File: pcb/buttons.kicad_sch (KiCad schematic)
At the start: 29 parts, among them SW1 SW_Push_SPDT, SW2 SW_Push_SPDT, SW3 SW_Push_SPDT, SW4 SW_Push_SPDT, SW5 RotaryEncoder

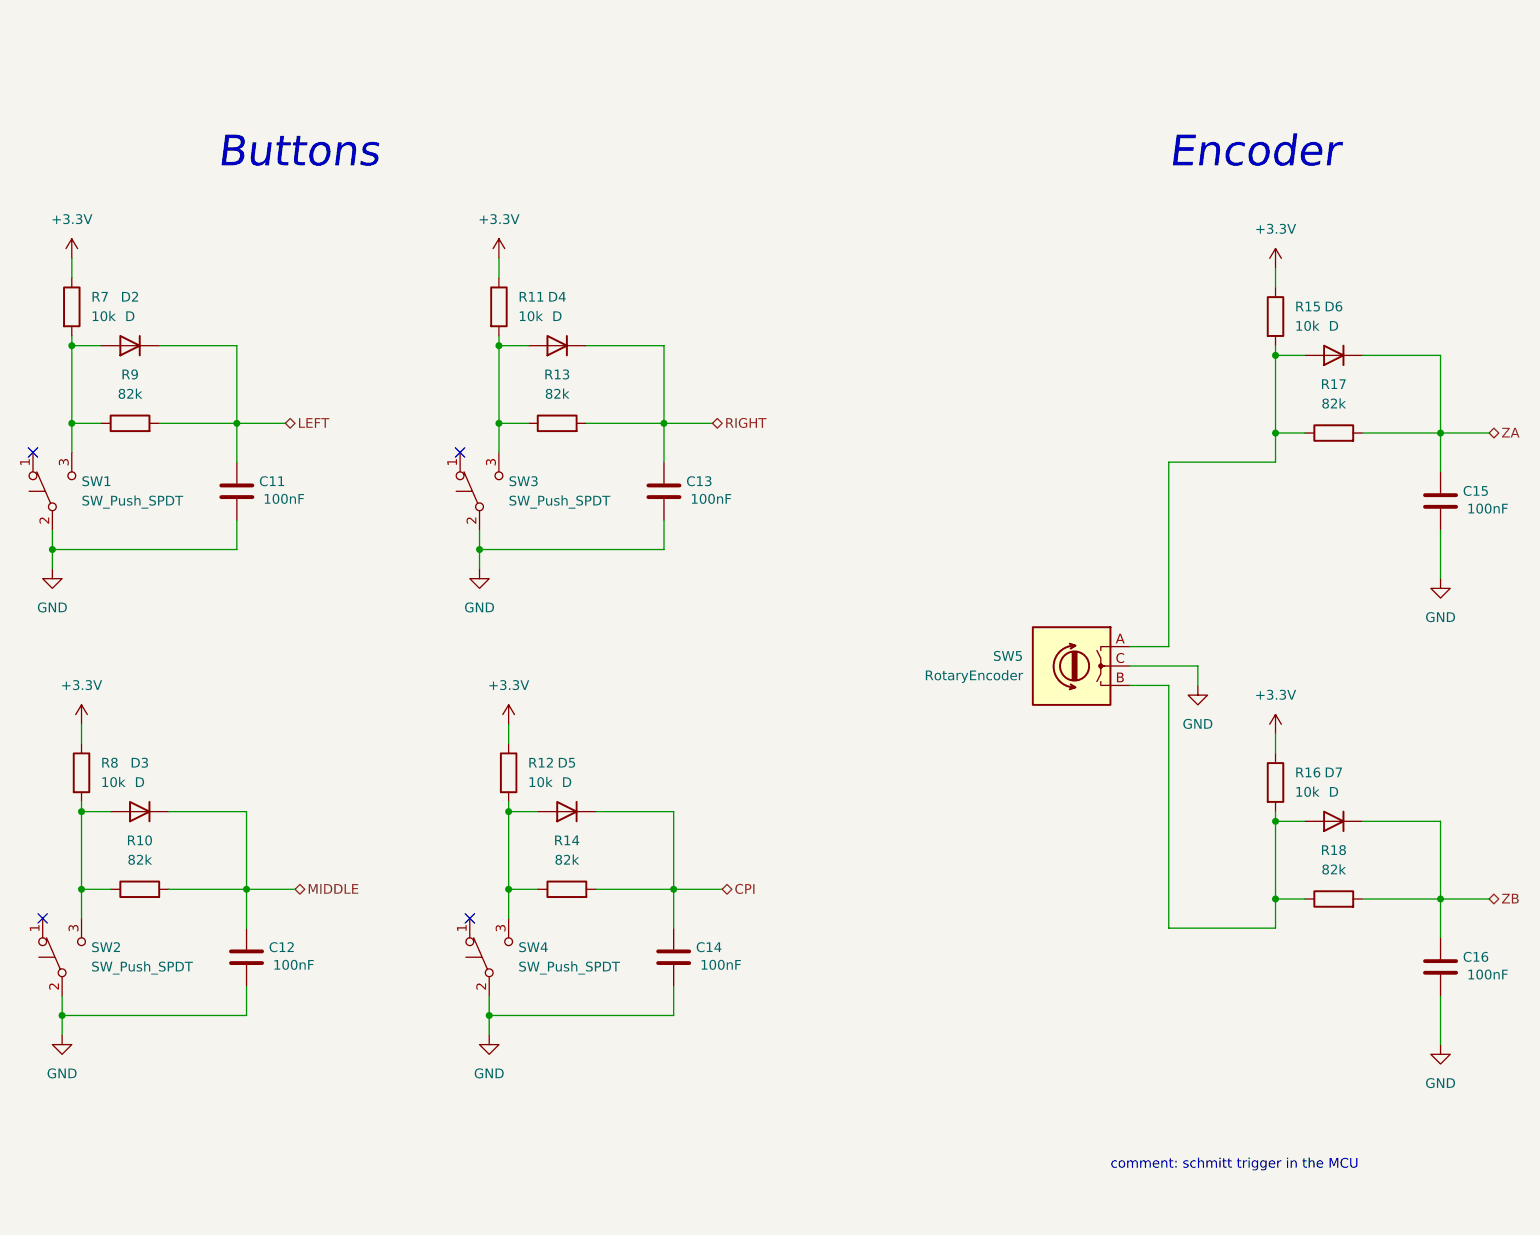
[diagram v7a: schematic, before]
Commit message: added PWR_FLAGs to pass ERC checks
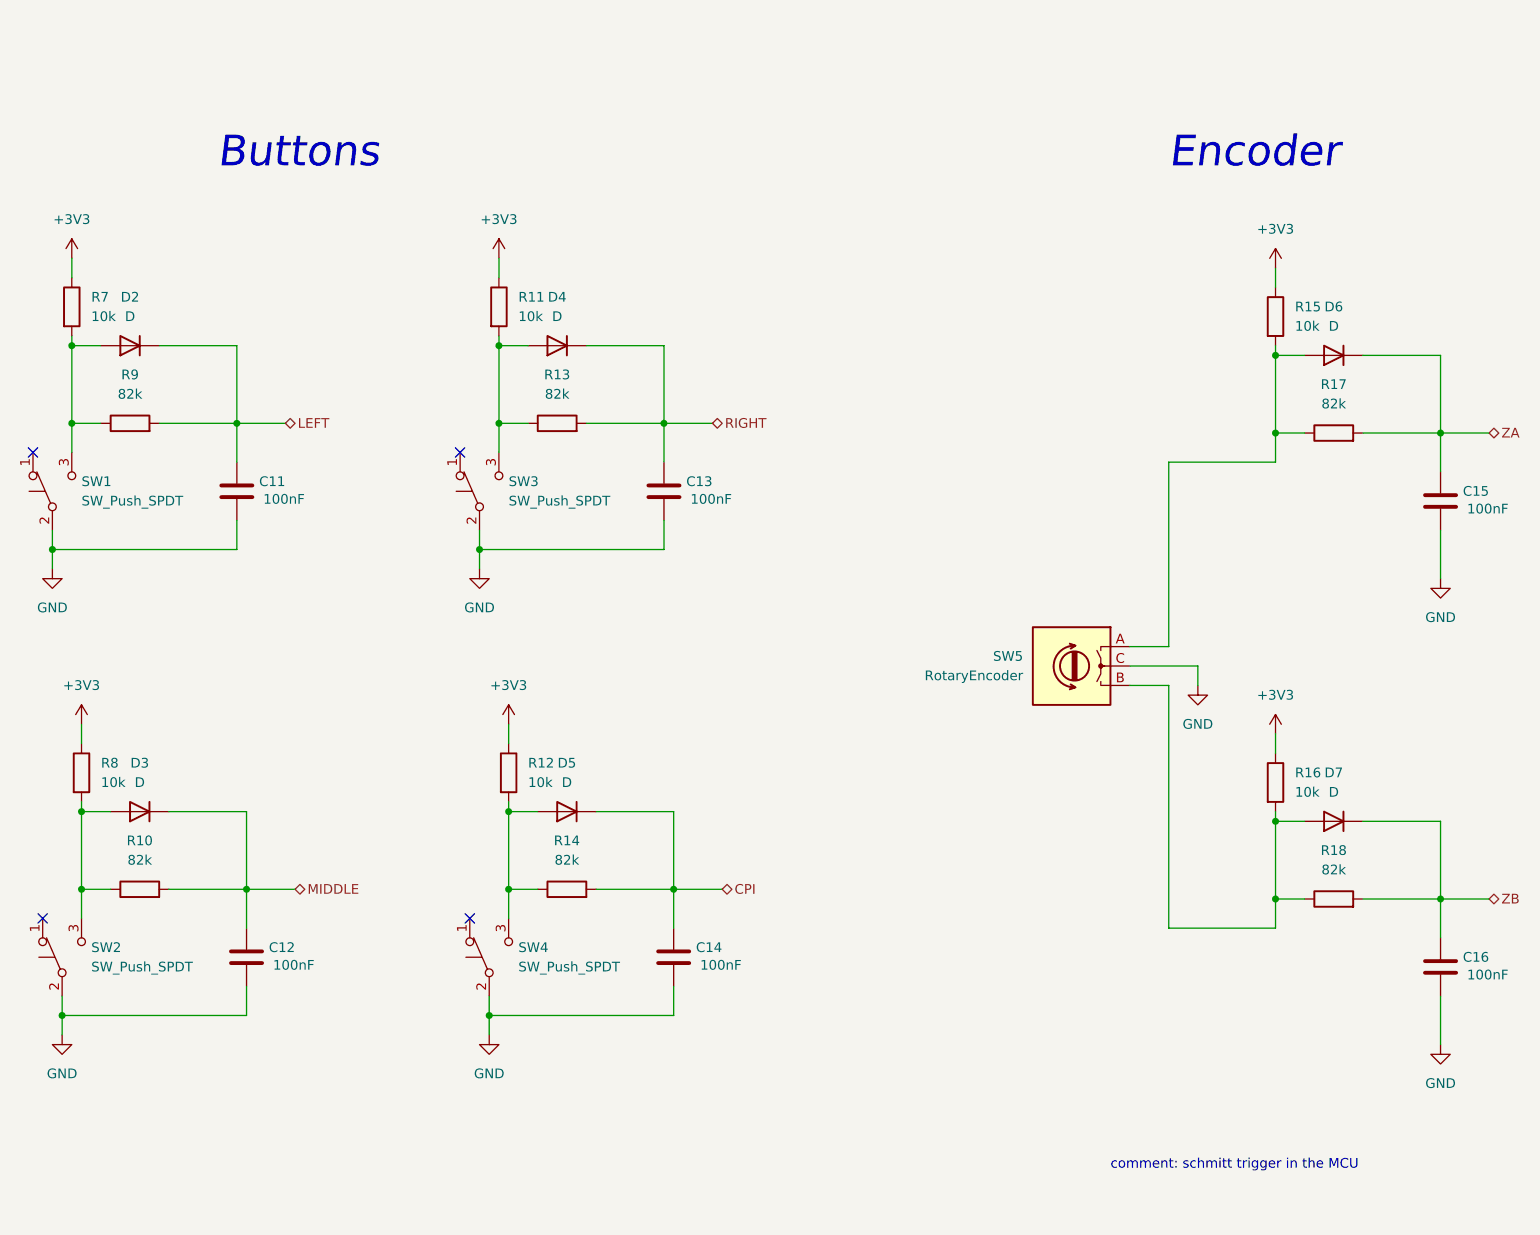
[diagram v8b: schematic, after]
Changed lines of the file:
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@@
     (stroke (width 0) (type default) (color 0 0 0 0))
   )
-  (wire (pts (xy 43.18 52.07) (xy 43.18 49.53))
+  (wire (pts (xy 43.18 49.53) (xy 43.18 52.07))
     (stroke (width 0) (type default) (color 0 0 0 0))
   )
@@
     (pin "1")
   )
+  (symbol (lib_id "power:+3V3") (at 200.66 50.8 0) (unit 1)
+    (in_bom yes) (on_board yes) (fields_autoplaced)
+    (property "Reference" "#PWR0105" (id 0) (at 200.66 54.61 0)
+      (effects (font (size 1.27 1.27)) hide)
+    )
+    (property "Value" "+3V3" (id 1) (at 200.66 45.72 0))
+    (property "Footprint" "" (id 2) (at 200.66 50.8 0)
+      (effects (font (size 1.27 1.27)) hide)
+    )
+    (property "Datasheet" "" (id 3) (at 200.66 50.8 0)
+      (effects (font (size 1.27 1.27)) hide)
+    )
+    (pin "1")
+  )
   (symbol (lib_id "power:GND") (at 222.25 152.4 0) (mirror y) (unit 1)
     (in_bom yes) (on_board yes)
@@
     (pin "2")
   )
-  (symbol (lib_id "power:+3.3V") (at 200.66 50.8 0) (unit 1)
-    (in_bom yes) (on_board yes) (fields_autoplaced)
-    (property "Reference" "#PWR032" (id 0) (at 200.66 54.61 0)
-      (effects (font (size 1.27 1.27)) hide)
-    )
-    (property "Value" "+3.3V" (id 1) (at 200.66 45.72 0))
-    (property "Footprint" "" (id 2) (at 200.66 50.8 0)
-      (effects (font (size 1.27 1.27)) hide)
-    )
-    (property "Datasheet" "" (id 3) (at 200.66 50.8 0)
-      (effects (font (size 1.27 1.27)) hide)
-    )
-    (pin "1")
-  )
   (symbol (lib_id "Device:C") (at 121.92 140.97 0) (mirror y) (unit 1)
     (in_bom yes) (on_board yes)
@@
     (pin "C")
   )
-  (symbol (lib_id "power:+3.3V") (at 99.06 49.53 0) (unit 1)
-    (in_bom yes) (on_board yes) (fields_autoplaced)
-    (property "Reference" "#PWR029" (id 0) (at 99.06 53.34 0)
-      (effects (font (size 1.27 1.27)) hide)
-    )
-    (property "Value" "+3.3V" (id 1) (at 99.06 44.45 0))
-    (property "Footprint" "" (id 2) (at 99.06 49.53 0)
-      (effects (font (size 1.27 1.27)) hide)
-    )
-    (property "Datasheet" "" (id 3) (at 99.06 49.53 0)
-      (effects (font (size 1.27 1.27)) hide)
-    )
-    (pin "1")
-  )
   (symbol (lib_id "Device:D") (at 52.07 121.92 180) (unit 1)
     (in_bom yes) (on_board yes) (fields_autoplaced)
@@
     (pin "2")
   )
+  (symbol (lib_id "power:+3V3") (at 100.33 110.49 0) (unit 1)
+    (in_bom yes) (on_board yes) (fields_autoplaced)
+    (property "Reference" "#PWR0101" (id 0) (at 100.33 114.3 0)
+      (effects (font (size 1.27 1.27)) hide)
+    )
+    (property "Value" "+3V3" (id 1) (at 100.33 105.41 0))
+    (property "Footprint" "" (id 2) (at 100.33 110.49 0)
+      (effects (font (size 1.27 1.27)) hide)
+    )
+    (property "Datasheet" "" (id 3) (at 100.33 110.49 0)
+      (effects (font (size 1.27 1.27)) hide)
+    )
+    (pin "1")
+  )
   (symbol (lib_id "Device:R") (at 106.68 71.12 90) (unit 1)
     (in_bom yes) (on_board yes)
@@
     (pin "2")
   )
-  (symbol (lib_id "power:+3.3V") (at 44.45 110.49 0) (unit 1)
-    (in_bom yes) (on_board yes) (fields_autoplaced)
-    (property "Reference" "#PWR026" (id 0) (at 44.45 114.3 0)
-      (effects (font (size 1.27 1.27)) hide)
-    )
-    (property "Value" "+3.3V" (id 1) (at 44.45 105.41 0))
-    (property "Footprint" "" (id 2) (at 44.45 110.49 0)
-      (effects (font (size 1.27 1.27)) hide)
-    )
-    (property "Datasheet" "" (id 3) (at 44.45 110.49 0)
-      (effects (font (size 1.27 1.27)) hide)
-    )
-    (pin "1")
-  )
   (symbol (lib_id "power:GND") (at 40.64 90.17 0) (mirror y) (unit 1)
     (in_bom yes) (on_board yes)
@@
     (pin "1")
   )
+  (symbol (lib_id "power:+3V3") (at 43.18 49.53 0) (unit 1)
+    (in_bom yes) (on_board yes) (fields_autoplaced)
+    (property "Reference" "#PWR0102" (id 0) (at 43.18 53.34 0)
+      (effects (font (size 1.27 1.27)) hide)
+    )
+    (property "Value" "+3V3" (id 1) (at 43.18 44.45 0))
+    (property "Footprint" "" (id 2) (at 43.18 49.53 0)
+      (effects (font (size 1.27 1.27)) hide)
+    )
+    (property "Datasheet" "" (id 3) (at 43.18 49.53 0)
+      (effects (font (size 1.27 1.27)) hide)
+    )
+    (pin "1")
+  )
   (symbol (lib_id "Device:C") (at 222.25 81.28 0) (mirror y) (unit 1)
     (in_bom yes) (on_board yes)
@@
     (pin "1")
     (pin "2")
-  )
-  (symbol (lib_id "power:+3.3V") (at 100.33 110.49 0) (unit 1)
-    (in_bom yes) (on_board yes) (fields_autoplaced)
-    (property "Reference" "#PWR030" (id 0) (at 100.33 114.3 0)
-      (effects (font (size 1.27 1.27)) hide)
-    )
-    (property "Value" "+3.3V" (id 1) (at 100.33 105.41 0))
-    (property "Footprint" "" (id 2) (at 100.33 110.49 0)
-      (effects (font (size 1.27 1.27)) hide)
-    )
-    (property "Datasheet" "" (id 3) (at 100.33 110.49 0)
-      (effects (font (size 1.27 1.27)) hide)
-    )
-    (pin "1")
   )
   (symbol (lib_id "Device:D") (at 106.68 60.96 180) (unit 1)
@@
     (pin "3")
   )
-  (symbol (lib_id "power:+3.3V") (at 43.18 49.53 0) (unit 1)
-    (in_bom yes) (on_board yes) (fields_autoplaced)
-    (property "Reference" "#PWR025" (id 0) (at 43.18 53.34 0)
-      (effects (font (size 1.27 1.27)) hide)
-    )
-    (property "Value" "+3.3V" (id 1) (at 43.18 44.45 0))
-    (property "Footprint" "" (id 2) (at 43.18 49.53 0)
-      (effects (font (size 1.27 1.27)) hide)
-    )
-    (property "Datasheet" "" (id 3) (at 43.18 49.53 0)
+  (symbol (lib_id "power:+3V3") (at 99.06 49.53 0) (unit 1)
+    (in_bom yes) (on_board yes) (fields_autoplaced)
+    (property "Reference" "#PWR0106" (id 0) (at 99.06 53.34 0)
+      (effects (font (size 1.27 1.27)) hide)
+    )
+    (property "Value" "+3V3" (id 1) (at 99.06 44.45 0))
+    (property "Footprint" "" (id 2) (at 99.06 49.53 0)
+      (effects (font (size 1.27 1.27)) hide)
+    )
+    (property "Datasheet" "" (id 3) (at 99.06 49.53 0)
       (effects (font (size 1.27 1.27)) hide)
     )
@@
     (pin "1")
   )
+  (symbol (lib_id "power:+3V3") (at 44.45 110.49 0) (unit 1)
+    (in_bom yes) (on_board yes) (fields_autoplaced)
+    (property "Reference" "#PWR0104" (id 0) (at 44.45 114.3 0)
+      (effects (font (size 1.27 1.27)) hide)
+    )
+    (property "Value" "+3V3" (id 1) (at 44.45 105.41 0))
+    (property "Footprint" "" (id 2) (at 44.45 110.49 0)
+      (effects (font (size 1.27 1.27)) hide)
+    )
+    (property "Datasheet" "" (id 3) (at 44.45 110.49 0)
+      (effects (font (size 1.27 1.27)) hide)
+    )
+    (pin "1")
+  )
   (symbol (lib_id "Device:C") (at 66.04 140.97 0) (mirror y) (unit 1)
     (in_bom yes) (on_board yes)
@@
     (pin "1")
     (pin "2")
+  )
+  (symbol (lib_id "power:+3V3") (at 200.66 111.76 0) (unit 1)
+    (in_bom yes) (on_board yes) (fields_autoplaced)
+    (property "Reference" "#PWR0103" (id 0) (at 200.66 115.57 0)
+      (effects (font (size 1.27 1.27)) hide)
+    )
+    (property "Value" "+3V3" (id 1) (at 200.66 106.68 0))
+    (property "Footprint" "" (id 2) (at 200.66 111.76 0)
+      (effects (font (size 1.27 1.27)) hide)
+    )
+    (property "Datasheet" "" (id 3) (at 200.66 111.76 0)
+      (effects (font (size 1.27 1.27)) hide)
+    )
+    (pin "1")
   )
   (symbol (lib_id "Switch:SW_Push_SPDT") (at 40.64 80.01 90) (unit 1)
@@
     (pin "3")
   )
-  (symbol (lib_id "power:+3.3V") (at 200.66 111.76 0) (unit 1)
-    (in_bom yes) (on_board yes) (fields_autoplaced)
-    (property "Reference" "#PWR033" (id 0) (at 200.66 115.57 0)
-      (effects (font (size 1.27 1.27)) hide)
-    )
-    (property "Value" "+3.3V" (id 1) (at 200.66 106.68 0))
-    (property "Footprint" "" (id 2) (at 200.66 111.76 0)
-      (effects (font (size 1.27 1.27)) hide)
-    )
-    (property "Datasheet" "" (id 3) (at 200.66 111.76 0)
-      (effects (font (size 1.27 1.27)) hide)
-    )
-    (pin "1")
-  )
   (symbol (lib_id "power:GND") (at 96.52 90.17 0) (mirror y) (unit 1)
